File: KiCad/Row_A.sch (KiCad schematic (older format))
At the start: 28 parts, among them U10 RGB_WS2812B, U11 RGB_WS2812B, U12 RGB_WS2812B, U13 RGB_WS2812B, U14 RGB_WS2812B, U15 RGB_WS2812B, U2 RGB_WS2812B, U3 RGB_WS2812B, U4 RGB_WS2812B, U5 RGB_WS2812B, U6 RGB_WS2812B, U7 RGB_WS2812B, U8 RGB_WS2812B, U9 RGB_WS2812B

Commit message: Board layout updated
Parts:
- removed U10, U11, U12, U13, U14, U15, U3, U4, U5, U6, U7, U8, U9: RGB_WS2812B, symbol RGB_WS2812B
- removed U2: RGB_WS2812B, ~, symbol RGB_WS2812B
- added LED1, LED10, LED11, LED12, LED13, LED14, LED2, LED3, LED4, LED5, LED6, LED7, LED8, LED9: WS2812B, ~, symbol WS2812B
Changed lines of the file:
@@
 Sheet 2 14
 Title "ClockFOUR"
-Date "1 oct 2014"
+Date "2 oct 2014"
 Rev ""
 Comp "WyoLum"
@@
 F 11 "http://www.digikey.com/product-detail/en/C0805C104K3RACTU/399-1168-1-ND/411443" H 1700 3450 60  0001 L CNN "Field11"
 	1    1700 2550
-	1    0    0    -1
-$EndComp
-$Comp
-L RGB_WS2812B U2
-U 1 1 5424CDC4
-P 1525 1575
-F 0 "U2" V 1275 1575 60  0000 C CNN
-F 1 "RGB_WS2812B" V 1925 1575 60  0000 C CNN
-F 2 "~" H 1525 1575 60  0000 C CNN
-F 3 "" H 1525 1575 60  0000 C CNN
-	1    1525 1575
-	1    0    0    -1
-$EndComp
-$Comp
-L RGB_WS2812B U3
-U 1 1 5424CE47
-P 2925 1575
-F 0 "U3" V 2675 1575 60  0000 C CNN
-F 1 "RGB_WS2812B" V 3325 1575 60  0000 C CNN
-F 2 "" H 2925 1575 60  0000 C CNN
-F 3 "" H 2925 1575 60  0000 C CNN
-	1    2925 1575
-	1    0    0    -1
-$EndComp
-$Comp
-L RGB_WS2812B U4
-U 1 1 5424CE4D
-P 4325 1575
-F 0 "U4" V 4075 1575 60  0000 C CNN
-F 1 "RGB_WS2812B" V 4725 1575 60  0000 C CNN
-F 2 "" H 4325 1575 60  0000 C CNN
-F 3 "" H 4325 1575 60  0000 C CNN
-	1    4325 1575
-	1    0    0    -1
-$EndComp
-$Comp
-L RGB_WS2812B U5
-U 1 1 5424CE53
-P 5725 1575
-F 0 "U5" V 5475 1575 60  0000 C CNN
-F 1 "RGB_WS2812B" V 6125 1575 60  0000 C CNN
-F 2 "" H 5725 1575 60  0000 C CNN
-F 3 "" H 5725 1575 60  0000 C CNN
-	1    5725 1575
-	1    0    0    -1
-$EndComp
-$Comp
-L RGB_WS2812B U6
-U 1 1 5424CE59
-P 7125 1575
-F 0 "U6" V 6875 1575 60  0000 C CNN
-F 1 "RGB_WS2812B" V 7525 1575 60  0000 C CNN
-F 2 "" H 7125 1575 60  0000 C CNN
-F 3 "" H 7125 1575 60  0000 C CNN
-	1    7125 1575
-	1    0    0    -1
-$EndComp
-$Comp
-L RGB_WS2812B U7
-U 1 1 5424CE5F
-P 8525 1575
-F 0 "U7" V 8275 1575 60  0000 C CNN
-F 1 "RGB_WS2812B" V 8925 1575 60  0000 C CNN
-F 2 "" H 8525 1575 60  0000 C CNN
-F 3 "" H 8525 1575 60  0000 C CNN
-	1    8525 1575
-	1    0    0    -1
-$EndComp
-$Comp
-L RGB_WS2812B U8
-U 1 1 5424CE65
-P 9925 1575
-F 0 "U8" V 9675 1575 60  0000 C CNN
-F 1 "RGB_WS2812B" V 10325 1575 60  0000 C CNN
-F 2 "" H 9925 1575 60  0000 C CNN
-F 3 "" H 9925 1575 60  0000 C CNN
-	1    9925 1575
-	1    0    0    -1
-$EndComp
-$Comp
-L RGB_WS2812B U9
-U 1 1 5424CE6B
-P 1525 3975
-F 0 "U9" V 1275 3975 60  0000 C CNN
-F 1 "RGB_WS2812B" V 1925 3975 60  0000 C CNN
-F 2 "" H 1525 3975 60  0000 C CNN
-F 3 "" H 1525 3975 60  0000 C CNN
-	1    1525 3975
-	1    0    0    -1
-$EndComp
-$Comp
-L RGB_WS2812B U10
-U 1 1 5424CE71
-P 2925 3975
-F 0 "U10" V 2675 3975 60  0000 C CNN
-F 1 "RGB_WS2812B" V 3325 3975 60  0000 C CNN
-F 2 "" H 2925 3975 60  0000 C CNN
-F 3 "" H 2925 3975 60  0000 C CNN
-	1    2925 3975
-	1    0    0    -1
-$EndComp
-$Comp
-L RGB_WS2812B U11
-U 1 1 5424CE77
-P 4325 3975
-F 0 "U11" V 4075 3975 60  0000 C CNN
-F 1 "RGB_WS2812B" V 4725 3975 60  0000 C CNN
-F 2 "" H 4325 3975 60  0000 C CNN
-F 3 "" H 4325 3975 60  0000 C CNN
-	1    4325 3975
-	1    0    0    -1
-$EndComp
-$Comp
-L RGB_WS2812B U12
-U 1 1 5424CE7D
-P 5725 3975
-F 0 "U12" V 5475 3975 60  0000 C CNN
-F 1 "RGB_WS2812B" V 6125 3975 60  0000 C CNN
-F 2 "" H 5725 3975 60  0000 C CNN
-F 3 "" H 5725 3975 60  0000 C CNN
-	1    5725 3975
-	1    0    0    -1
-$EndComp
-$Comp
-L RGB_WS2812B U13
-U 1 1 5424CE83
-P 7125 3975
-F 0 "U13" V 6875 3975 60  0000 C CNN
-F 1 "RGB_WS2812B" V 7525 3975 60  0000 C CNN
-F 2 "" H 7125 3975 60  0000 C CNN
-F 3 "" H 7125 3975 60  0000 C CNN
-	1    7125 3975
-	1    0    0    -1
-$EndComp
-$Comp
-L RGB_WS2812B U14
-U 1 1 5424CE89
-P 8525 3975
-F 0 "U14" V 8275 3975 60  0000 C CNN
-F 1 "RGB_WS2812B" V 8925 3975 60  0000 C CNN
-F 2 "" H 8525 3975 60  0000 C CNN
-F 3 "" H 8525 3975 60  0000 C CNN
-	1    8525 3975
-	1    0    0    -1
-$EndComp
-$Comp
-L RGB_WS2812B U15
-U 1 1 5424CE8F
-P 9925 3975
-F 0 "U15" V 9675 3975 60  0000 C CNN
-F 1 "RGB_WS2812B" V 10325 3975 60  0000 C CNN
-F 2 "" H 9925 3975 60  0000 C CNN
-F 3 "" H 9925 3975 60  0000 C CNN
-	1    9925 3975
 	1    0    0    -1
 $EndComp
@@
 Connection ~ 1250 2350
 Connection ~ 10000 5100
+$Comp
+L WS2812B LED1
+U 1 1 542DED2D
+P 1525 1575
+F 0 "LED1" V 1275 1575 60  0000 C CNN
+F 1 "WS2812B" V 1925 1575 60  0001 C CNN
+F 2 "~" H 1525 1575 60  0000 C CNN
+F 3 "~" H 1525 1575 60  0000 C CNN
+	1    1525 1575
+	1    0    0    -1
+$EndComp
+$Comp
+L WS2812B LED2
+U 1 1 542DED3A
+P 2925 1575
+F 0 "LED2" V 2675 1575 60  0000 C CNN
+F 1 "WS2812B" V 3325 1575 60  0001 C CNN
+F 2 "~" H 2925 1575 60  0000 C CNN
+F 3 "~" H 2925 1575 60  0000 C CNN
+	1    2925 1575
+	1    0    0    -1
+$EndComp
+$Comp
+L WS2812B LED3
+U 1 1 542DED40
+P 4325 1575
+F 0 "LED3" V 4075 1575 60  0000 C CNN
+F 1 "WS2812B" V 4725 1575 60  0001 C CNN
+F 2 "~" H 4325 1575 60  0000 C CNN
+F 3 "~" H 4325 1575 60  0000 C CNN
+	1    4325 1575
+	1    0    0    -1
+$EndComp
+$Comp
+L WS2812B LED4
+U 1 1 542DED46
+P 5725 1575
+F 0 "LED4" V 5475 1575 60  0000 C CNN
+F 1 "WS2812B" V 6125 1575 60  0001 C CNN
+F 2 "~" H 5725 1575 60  0000 C CNN
+F 3 "~" H 5725 1575 60  0000 C CNN
+	1    5725 1575
+	1    0    0    -1
+$EndComp
+$Comp
+L WS2812B LED5
+U 1 1 542DED4C
+P 7125 1575
+F 0 "LED5" V 6875 1575 60  0000 C CNN
+F 1 "WS2812B" V 7525 1575 60  0001 C CNN
+F 2 "~" H 7125 1575 60  0000 C CNN
+F 3 "~" H 7125 1575 60  0000 C CNN
+	1    7125 1575
+	1    0    0    -1
+$EndComp
+$Comp
+L WS2812B LED6
+U 1 1 542DED52
+P 8525 1575
+F 0 "LED6" V 8275 1575 60  0000 C CNN
+F 1 "WS2812B" V 8925 1575 60  0001 C CNN
+F 2 "~" H 8525 1575 60  0000 C CNN
+F 3 "~" H 8525 1575 60  0000 C CNN
+	1    8525 1575
+	1    0    0    -1
+$EndComp
+$Comp
+L WS2812B LED7
+U 1 1 542DED58
+P 9925 1575
+F 0 "LED7" V 9675 1575 60  0000 C CNN
+F 1 "WS2812B" V 10325 1575 60  0001 C CNN
+F 2 "~" H 9925 1575 60  0000 C CNN
+F 3 "~" H 9925 1575 60  0000 C CNN
+	1    9925 1575
+	1    0    0    -1
+$EndComp
+$Comp
+L WS2812B LED8
+U 1 1 542DED5E
+P 1525 3975
+F 0 "LED8" V 1275 3975 60  0000 C CNN
+F 1 "WS2812B" V 1925 3975 60  0001 C CNN
+F 2 "~" H 1525 3975 60  0000 C CNN
+F 3 "~" H 1525 3975 60  0000 C CNN
+	1    1525 3975
+	1    0    0    -1
+$EndComp
+$Comp
+L WS2812B LED9
+U 1 1 542DED64
+P 2925 3975
+F 0 "LED9" V 2675 3975 60  0000 C CNN
+F 1 "WS2812B" V 3325 3975 60  0001 C CNN
+F 2 "~" H 2925 3975 60  0000 C CNN
+F 3 "~" H 2925 3975 60  0000 C CNN
+	1    2925 3975
+	1    0    0    -1
+$EndComp
+$Comp
+L WS2812B LED10
+U 1 1 542DED6A
+P 4325 3975
+F 0 "LED10" V 4075 3975 60  0000 C CNN
+F 1 "WS2812B" V 4725 3975 60  0001 C CNN
+F 2 "~" H 4325 3975 60  0000 C CNN
+F 3 "~" H 4325 3975 60  0000 C CNN
+	1    4325 3975
+	1    0    0    -1
+$EndComp
+$Comp
+L WS2812B LED11
+U 1 1 542DED70
+P 5725 3975
+F 0 "LED11" V 5475 3975 60  0000 C CNN
+F 1 "WS2812B" V 6125 3975 60  0001 C CNN
+F 2 "~" H 5725 3975 60  0000 C CNN
+F 3 "~" H 5725 3975 60  0000 C CNN
+	1    5725 3975
+	1    0    0    -1
+$EndComp
+$Comp
+L WS2812B LED12
+U 1 1 542DED76
+P 7125 3975
+F 0 "LED12" V 6875 3975 60  0000 C CNN
+F 1 "WS2812B" V 7525 3975 60  0001 C CNN
+F 2 "~" H 7125 3975 60  0000 C CNN
+F 3 "~" H 7125 3975 60  0000 C CNN
+	1    7125 3975
+	1    0    0    -1
+$EndComp
+$Comp
+L WS2812B LED13
+U 1 1 542DED7C
+P 8525 3975
+F 0 "LED13" V 8275 3975 60  0000 C CNN
+F 1 "WS2812B" V 8925 3975 60  0001 C CNN
+F 2 "~" H 8525 3975 60  0000 C CNN
+F 3 "~" H 8525 3975 60  0000 C CNN
+	1    8525 3975
+	1    0    0    -1
+$EndComp
+$Comp
+L WS2812B LED14
+U 1 1 542DED8C
+P 9925 3975
+F 0 "LED14" V 9675 3975 60  0000 C CNN
+F 1 "WS2812B" V 10325 3975 60  0001 C CNN
+F 2 "~" H 9925 3975 60  0000 C CNN
+F 3 "~" H 9925 3975 60  0000 C CNN
+	1    9925 3975
+	1    0    0    -1
+$EndComp
 $EndSCHEMATC

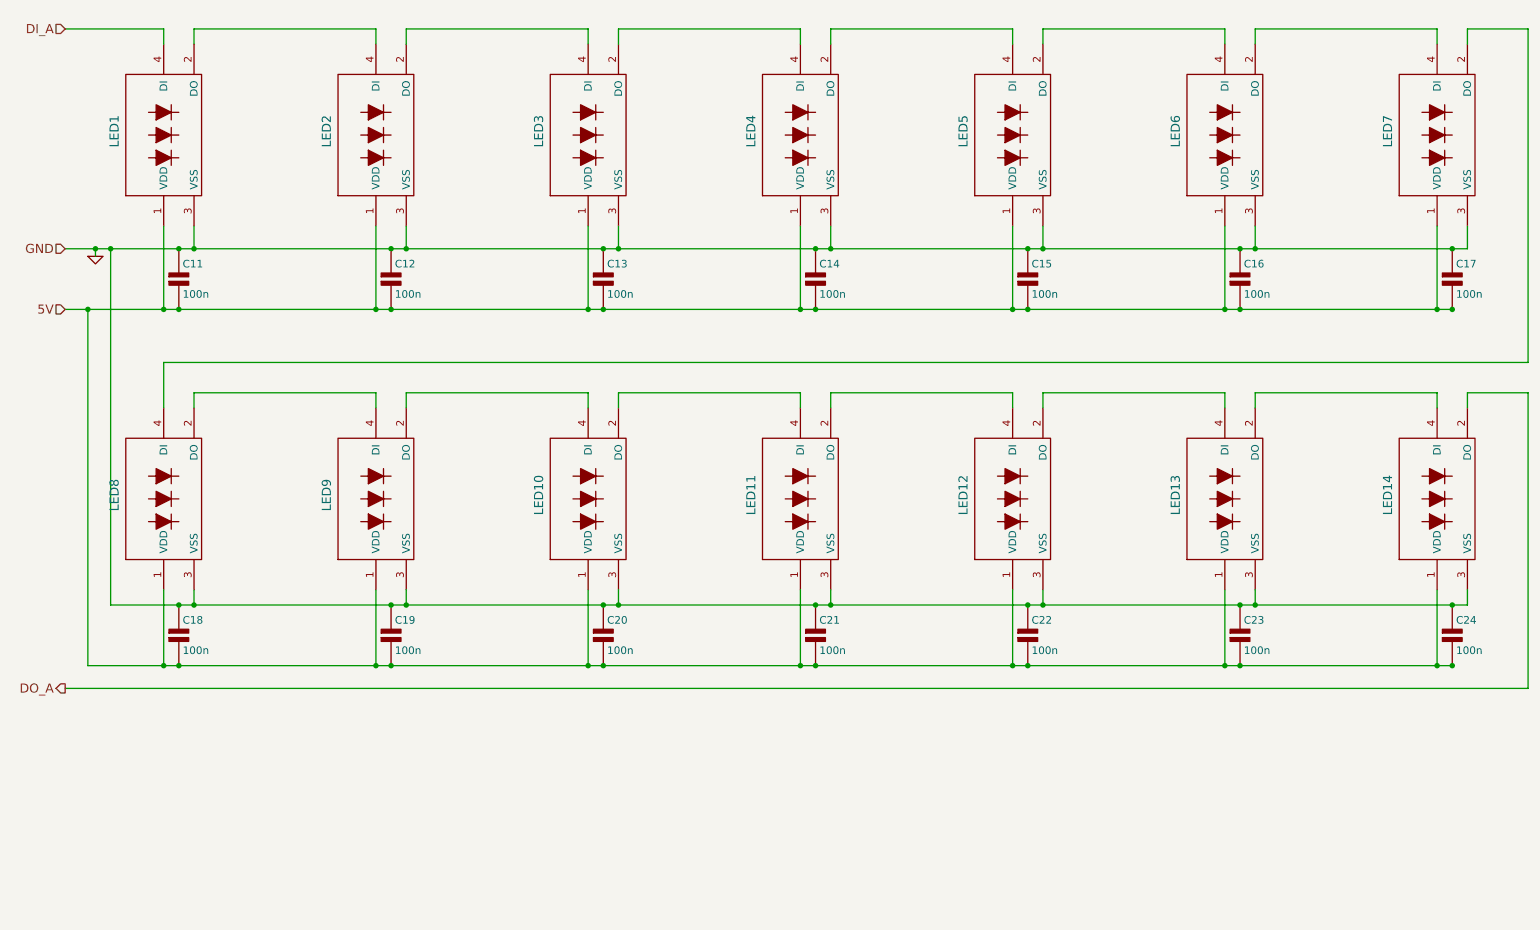
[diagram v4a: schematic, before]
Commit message: Board layout updated
Matrix placed and wired. Added RTC.
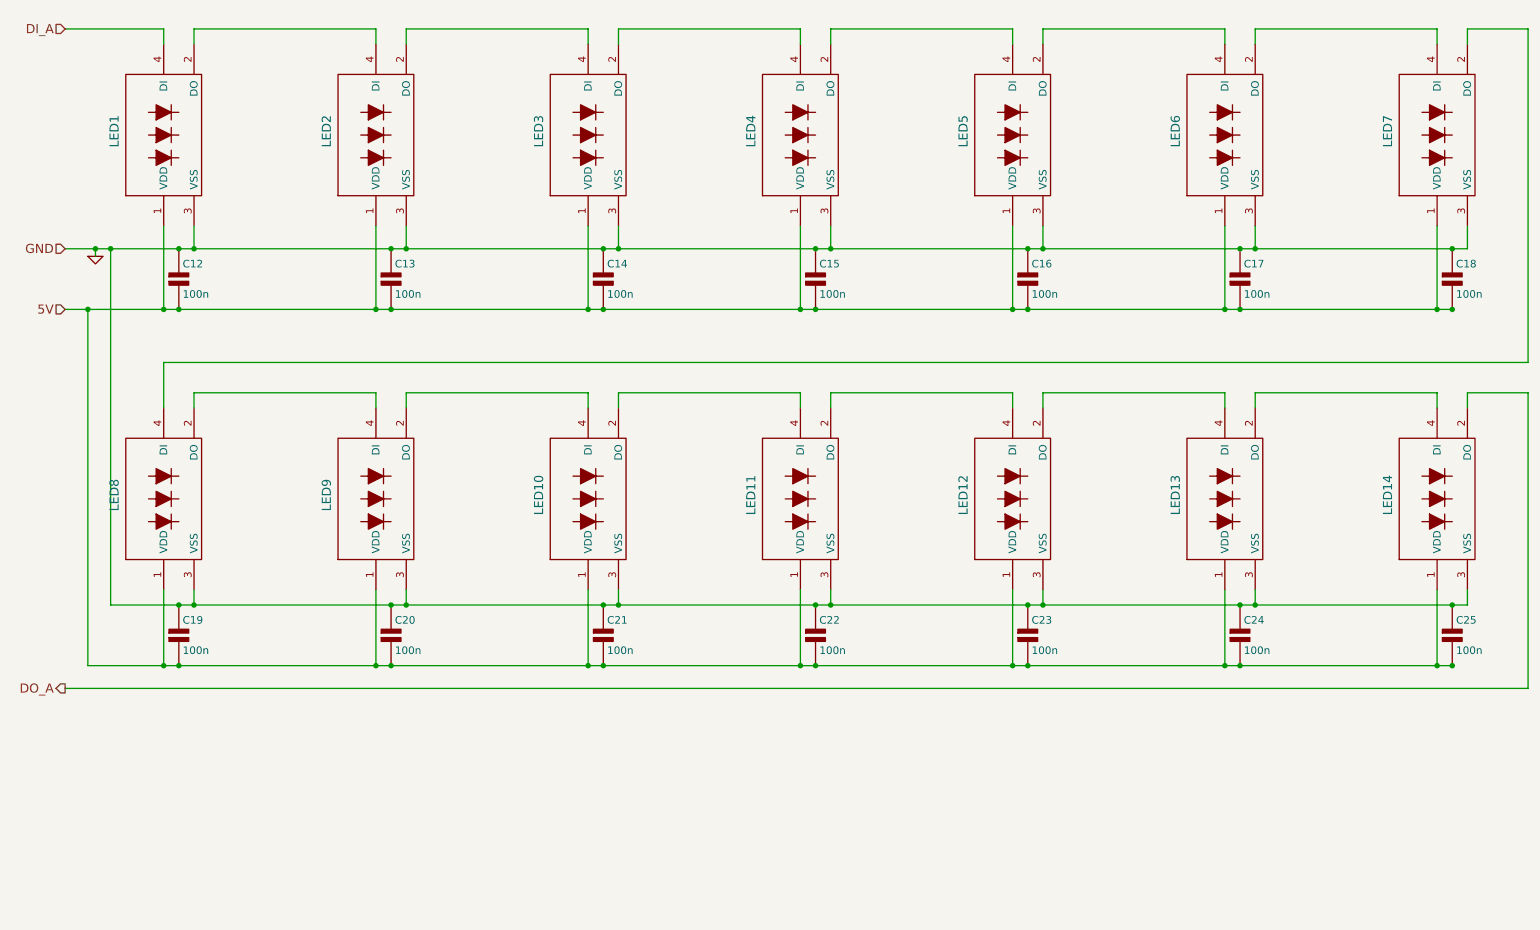
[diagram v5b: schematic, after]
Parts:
- renumbered C11 to C12, C12 to C13, C13 to C14, C14 to C15, C15 to C16, C16 to C17, C17 to C18, C18 to C19, C19 to C20, C20 to C21, C21 to C22, C22 to C23, C23 to C24, C24 to C25
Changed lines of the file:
@@
 Sheet 2 14
 Title "ClockFOUR"
-Date "2 oct 2014"
+Date "3 oct 2014"
 Rev ""
 Comp "WyoLum"
@@
 $EndComp
 $Comp
-L C2 C11
+L C2 C12
 U 1 1 5118AB57
 P 1700 2550
-F 0 "C11" H 1725 2650 50  0000 L CNN
+F 0 "C12" H 1725 2650 50  0000 L CNN
 F 1 "100n" H 1725 2450 50  0000 L CNN
 F 2 "TinyTiM_Lib:c_0805" H 1700 2550 50  0001 C CNN
@@
 Connection ~ 1600 2750
 $Comp
-L C2 C12
+L C2 C13
 U 1 1 5424D6B9
 P 3100 2550
-F 0 "C12" H 3125 2650 50  0000 L CNN
+F 0 "C13" H 3125 2650 50  0000 L CNN
 F 1 "100n" H 3125 2450 50  0000 L CNN
 F 2 "TinyTiM_Lib:c_0805" H 3100 2550 50  0001 C CNN
@@
 $EndComp
 $Comp
-L C2 C13
+L C2 C14
 U 1 1 5424D6C7
 P 4500 2550
-F 0 "C13" H 4525 2650 50  0000 L CNN
+F 0 "C14" H 4525 2650 50  0000 L CNN
 F 1 "100n" H 4525 2450 50  0000 L CNN
 F 2 "TinyTiM_Lib:c_0805" H 4500 2550 50  0001 C CNN
@@
 $EndComp
 $Comp
-L C2 C14
+L C2 C15
 U 1 1 5424D6D5
 P 5900 2550
-F 0 "C14" H 5925 2650 50  0000 L CNN
+F 0 "C15" H 5925 2650 50  0000 L CNN
 F 1 "100n" H 5925 2450 50  0000 L CNN
 F 2 "TinyTiM_Lib:c_0805" H 5900 2550 50  0001 C CNN
@@
 $EndComp
 $Comp
-L C2 C15
+L C2 C16
 U 1 1 5424D6E3
 P 7300 2550
-F 0 "C15" H 7325 2650 50  0000 L CNN
+F 0 "C16" H 7325 2650 50  0000 L CNN
 F 1 "100n" H 7325 2450 50  0000 L CNN
 F 2 "TinyTiM_Lib:c_0805" H 7300 2550 50  0001 C CNN
@@
 $EndComp
 $Comp
-L C2 C16
+L C2 C17
 U 1 1 5424D6F1
 P 8700 2550
-F 0 "C16" H 8725 2650 50  0000 L CNN
+F 0 "C17" H 8725 2650 50  0000 L CNN
 F 1 "100n" H 8725 2450 50  0000 L CNN
 F 2 "TinyTiM_Lib:c_0805" H 8700 2550 50  0001 C CNN
@@
 $EndComp
 $Comp
-L C2 C17
+L C2 C18
 U 1 1 5424D6FF
 P 10100 2550
-F 0 "C17" H 10125 2650 50  0000 L CNN
+F 0 "C18" H 10125 2650 50  0000 L CNN
 F 1 "100n" H 10125 2450 50  0000 L CNN
 F 2 "TinyTiM_Lib:c_0805" H 10100 2550 50  0001 C CNN
@@
 Connection ~ 10000 2750
 $Comp
-L C2 C18
+L C2 C19
 U 1 1 5424D75D
 P 1700 4900
-F 0 "C18" H 1725 5000 50  0000 L CNN
+F 0 "C19" H 1725 5000 50  0000 L CNN
 F 1 "100n" H 1725 4800 50  0000 L CNN
 F 2 "TinyTiM_Lib:c_0805" H 1700 4900 50  0001 C CNN
@@
 Connection ~ 1600 5100
 $Comp
-L C2 C19
+L C2 C20
 U 1 1 5424DFA1
 P 3100 4900
-F 0 "C19" H 3125 5000 50  0000 L CNN
+F 0 "C20" H 3125 5000 50  0000 L CNN
 F 1 "100n" H 3125 4800 50  0000 L CNN
 F 2 "TinyTiM_Lib:c_0805" H 3100 4900 50  0001 C CNN
@@
 $EndComp
 $Comp
-L C2 C20
+L C2 C21
 U 1 1 5424DFAF
 P 4500 4900
-F 0 "C20" H 4525 5000 50  0000 L CNN
+F 0 "C21" H 4525 5000 50  0000 L CNN
 F 1 "100n" H 4525 4800 50  0000 L CNN
 F 2 "TinyTiM_Lib:c_0805" H 4500 4900 50  0001 C CNN
@@
 $EndComp
 $Comp
-L C2 C21
+L C2 C22
 U 1 1 5424DFBD
 P 5900 4900
-F 0 "C21" H 5925 5000 50  0000 L CNN
+F 0 "C22" H 5925 5000 50  0000 L CNN
 F 1 "100n" H 5925 4800 50  0000 L CNN
 F 2 "TinyTiM_Lib:c_0805" H 5900 4900 50  0001 C CNN
@@
 $EndComp
 $Comp
-L C2 C22
+L C2 C23
 U 1 1 5424DFCB
 P 7300 4900
-F 0 "C22" H 7325 5000 50  0000 L CNN
+F 0 "C23" H 7325 5000 50  0000 L CNN
 F 1 "100n" H 7325 4800 50  0000 L CNN
 F 2 "TinyTiM_Lib:c_0805" H 7300 4900 50  0001 C CNN
@@
 $EndComp
 $Comp
-L C2 C23
+L C2 C24
 U 1 1 5424DFD9
 P 8700 4900
-F 0 "C23" H 8725 5000 50  0000 L CNN
+F 0 "C24" H 8725 5000 50  0000 L CNN
 F 1 "100n" H 8725 4800 50  0000 L CNN
 F 2 "TinyTiM_Lib:c_0805" H 8700 4900 50  0001 C CNN
@@
 $EndComp
 $Comp
-L C2 C24
+L C2 C25
 U 1 1 5424DFE7
 P 10100 4900
-F 0 "C24" H 10125 5000 50  0000 L CNN
+F 0 "C25" H 10125 5000 50  0000 L CNN
 F 1 "100n" H 10125 4800 50  0000 L CNN
 F 2 "TinyTiM_Lib:c_0805" H 10100 4900 50  0001 C CNN
